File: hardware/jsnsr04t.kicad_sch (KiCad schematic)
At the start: 12 parts, among them J1 SWD, J2 MOD_L, J3 JSN-SR04T, J4 MOD_R, U2 DS18B20, U3 5V LDO, U4 TXB0104D, U5 ATtiny1614-SS

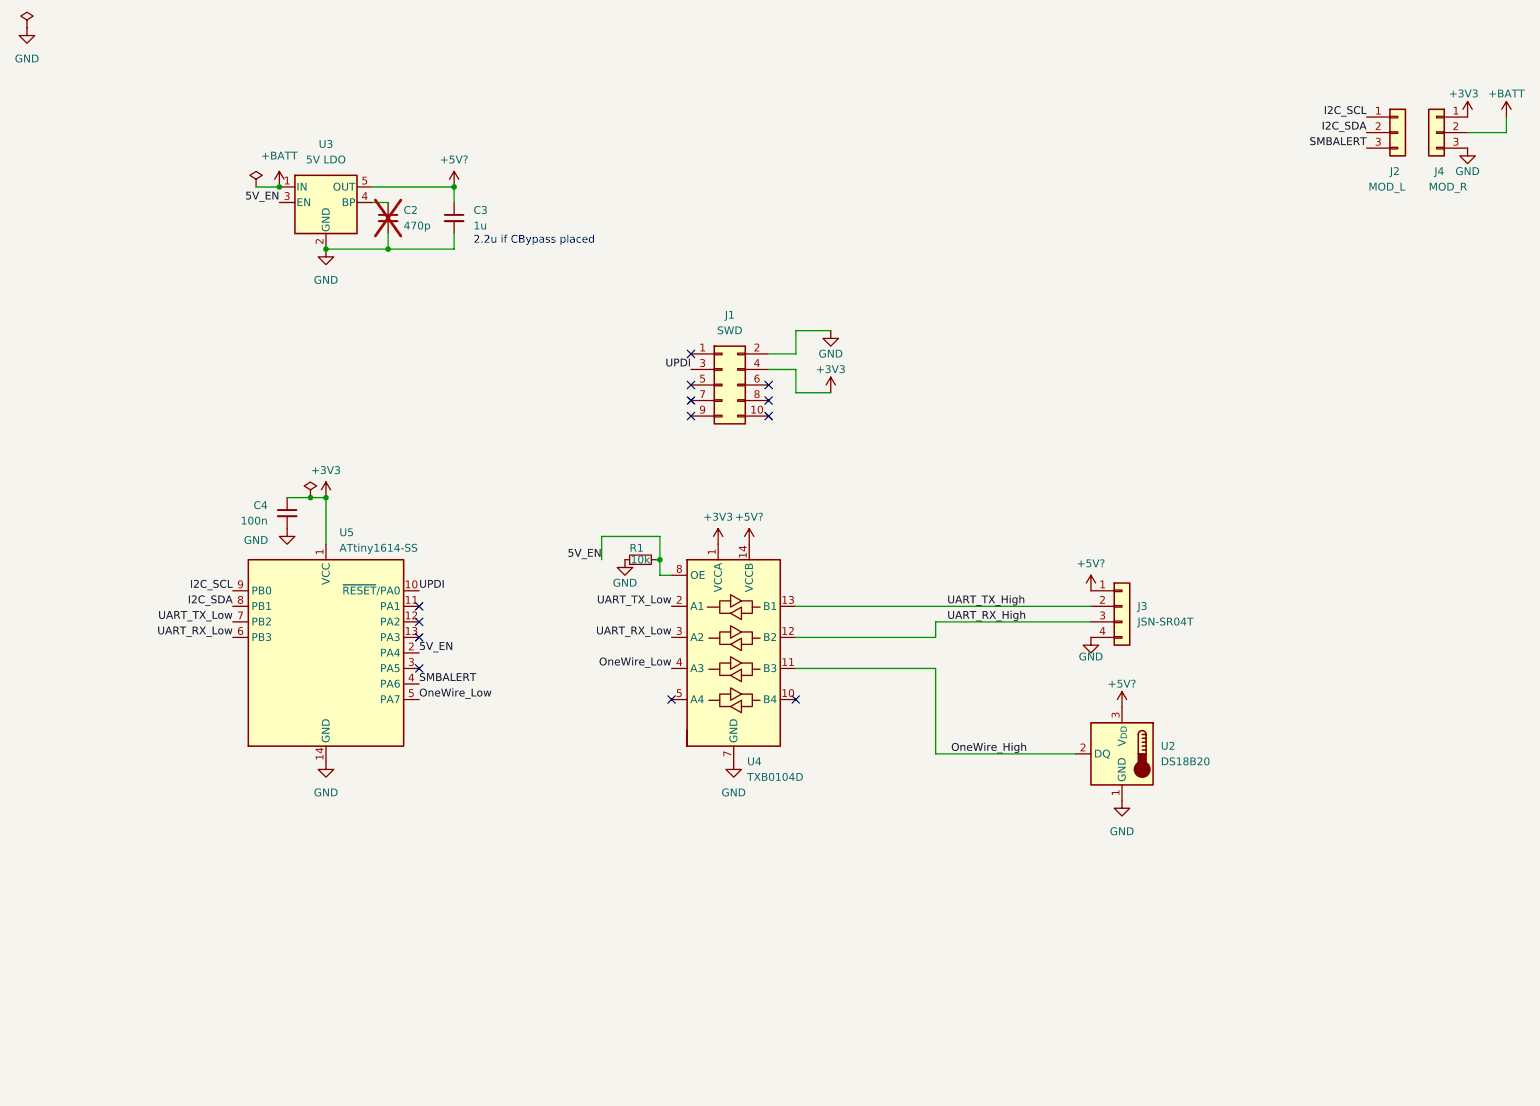
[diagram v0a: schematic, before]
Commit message: Include terminal blocks for DS18B20
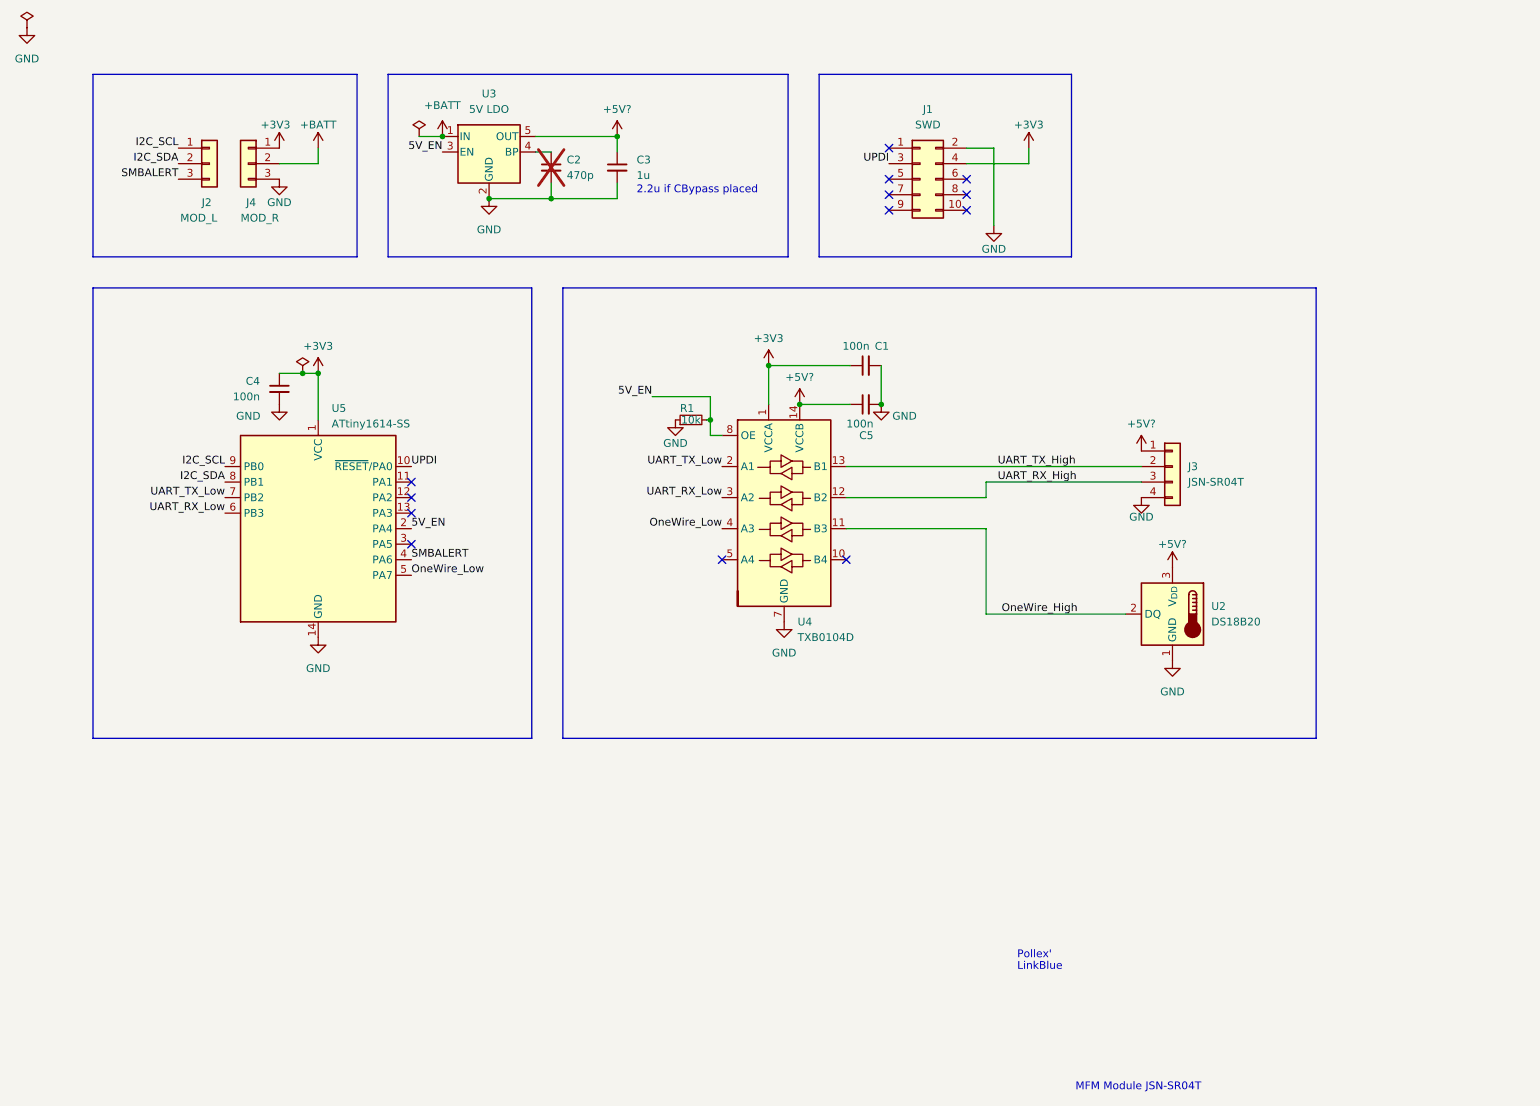
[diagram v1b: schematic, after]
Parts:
- added C1, C5: 100n, Capacitor_SMD:C_0603_1608Metric, symbol Device:C_Small
- U2: footprint Connector_JST:JST_PH_S3B-PH-K_1x03_P2.00mm_Horizontal -> Library:TE-Connectivity_3_pin_terminal_block
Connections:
- net +3V3: now also C1.1
- net +5V?: now also C5.1
- net GND: now also C1.2, C5.2
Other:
- note added: "LinkBlue"
- note added: "MFM Module JSN-SR04T"
- note added: "Pollex'"
- moved on the sheet: C2, C3, C4, J1, J2, J3, J4, R1, U2, U3, U4, U5

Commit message: Drive DS18B20 from IO Port\nRemove DS18B20 from level translator
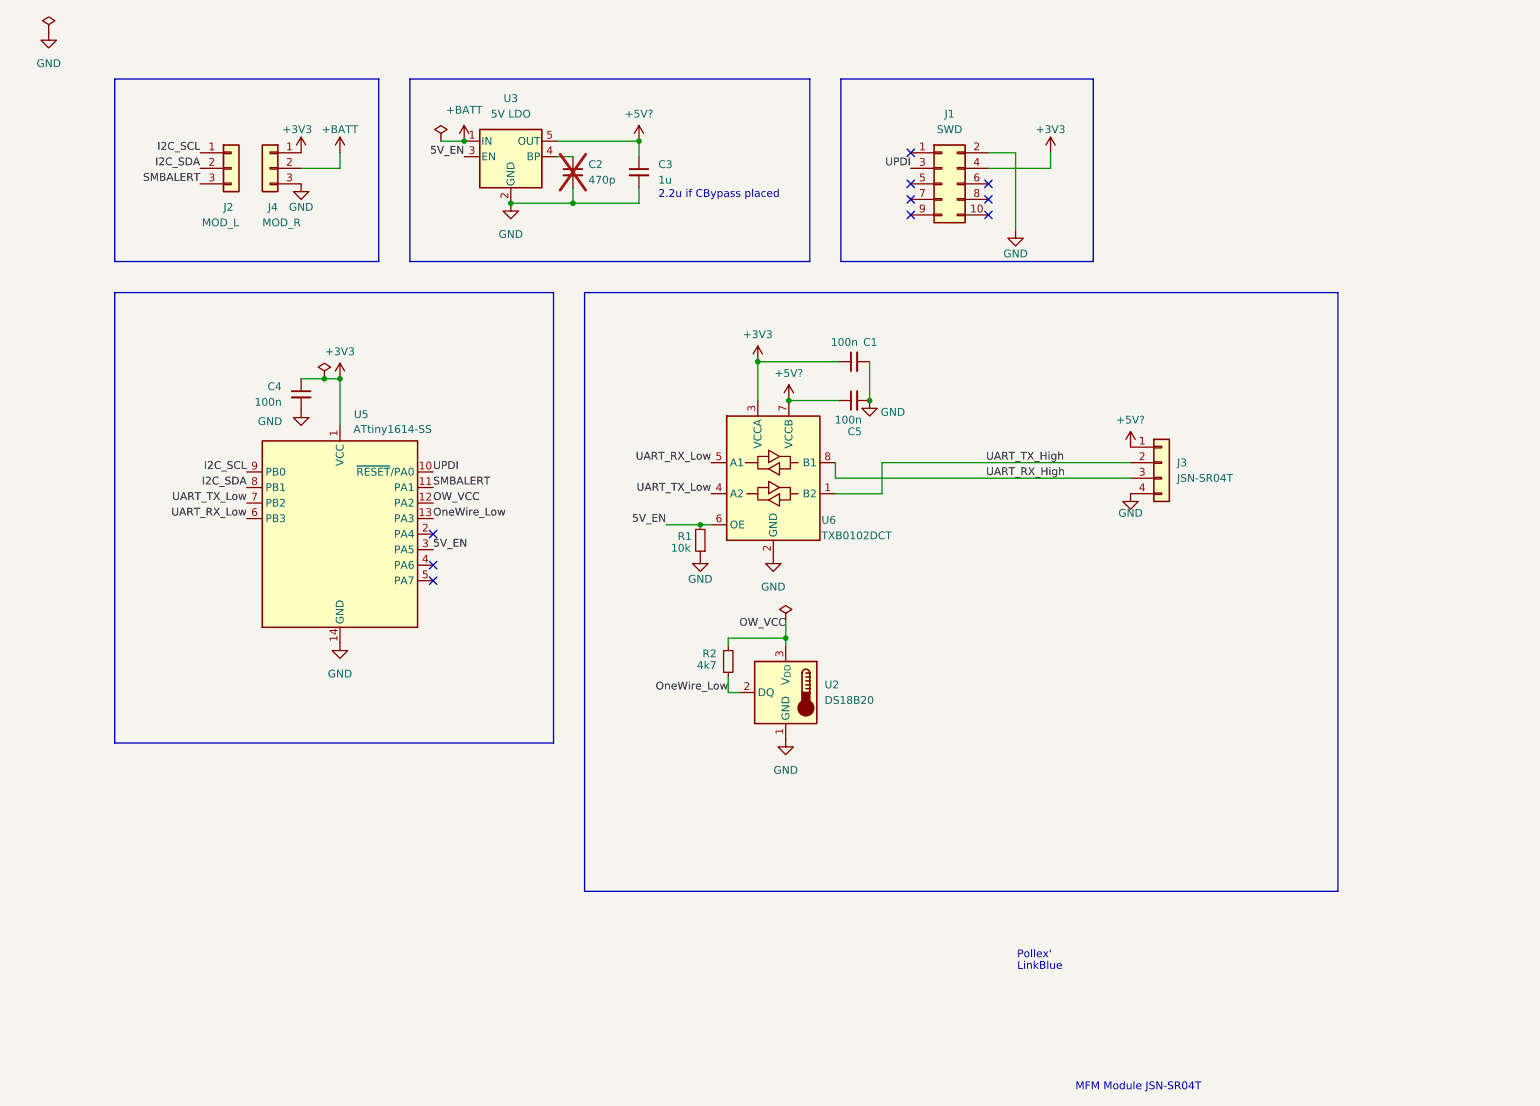
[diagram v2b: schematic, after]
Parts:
- removed U4: TXB0104D, Package_SO:SOIC-14_3.9x8.7mm_P1.27mm, symbol Logic_LevelTranslator:TXB0104D
- added R2: 4k7, Resistor_SMD:R_0603_1608Metric, symbol Device:R_Small
- added U6: TXB0102DCT, Package_SO:TSSOP-8_3x3mm_P0.65mm, symbol Logic_LevelTranslator:TXB0102DCT
- R1: footprint Capacitor_SMD:C_0603_1608Metric -> Resistor_SMD:R_0603_1608Metric
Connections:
- net OneWire_High is gone; now on net OneWire_Low: U2.2 (DQ)
- net +3V3: now also U6.3 (VCCA)
- net +5V?: now also U6.7 (VCCB); no longer U2.3 (V_{DD})
- net 5V_EN: now also U5.3 (PA5), U6.6 (OE); no longer U5.2 (PA4)
- net GND: now also U6.2 (GND)
- net OneWire_Low: now also U5.13 (PA3), R2.2; no longer U5.5 (PA7)
- net SMBALERT: now also U5.11 (PA1); no longer U5.4 (PA6)
- net UART_RX_High: now also U6.8 (B1)
- net UART_RX_Low: now also U6.5 (A1)
- net UART_TX_High: now also U6.1 (B2)
- net UART_TX_Low: now also U6.4 (A2)
- net OW_VCC: now reaches U5.12 (PA2)
- net OW_VCC: now also U2.3 (V_{DD}), R2.1
- no-connect marks 13 -> 10
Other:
- moved on the sheet: C1, C2, C3, C4, C5, J1, J2, J3, J4, R1, U2, U3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
